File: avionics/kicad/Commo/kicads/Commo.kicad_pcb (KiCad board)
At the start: 4 copper layers, 55 x 35 mm, 88 parts, among them U1 ByA 100nF +3V3 U1-VDDA Bypass, U1 ByB 100nF +3V3 U1-VDD Bypass

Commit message: docs(avionics): Wurth usage notice + uncrewed-only statement on 5 boards; catalogue REF-SENSOR-022..040
Owner decision 2026-09-26: retain the Wurth parts. The Wurth datasheet
usage notice is quoted verbatim [REF-SENSOR-028: Wurth 749010012A data
sheet rev 004.000 p.1] with an 'intended for use only on uncrewed
aircraft' statement in each Wurth-bearing board's .md, as a schematic
text item and PCB Cmts.User text, and in title-block comments 8/9
(tools/add_board_notices.py, idempotent). ERC/DRC/parity counts
unchanged on all five boards (kicad-cli 9.0.2).

REFERENCES.md: REF-SENSOR-022/023/025-030/033/038/040 were cited by
board schematics and generator scripts but never catalogued; entries
added with URLs validated 2026-09-26, unreachable ones marked
'requires verification'.

AI-authored: Claude Opus 5.5 (Anthropic).

Co-Authored-By: Claude Opus 5.5 <noreply@anthropic.com>
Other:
- board text added: "WÜRTH ELEKTRONIK USAGE NOTICE (verbatim, 749010012A data sheet rev 004.000 p.1; applies to Würth parts on this board: 749010012A, 742792510, 742792512): This electronic component has been designed and developed for usage in general electronic equipment only. This product is not authorized for use in equipment where a higher safety standard and reliability standard is especially required or where 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"
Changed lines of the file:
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@@
 		(comment 4 "EMI hardening: SRF2012 CMC + PRTR5V0U2X TVS + Wuerth 742792512 FB + X2Y 4.7nF cap")
 		(comment 5 "Hull: misubisu CC BY 4.0 | Firefly/Serenity fan-work, not officially licensed")
+		(comment 8 "Wurth parts (749010012A, 742792510, 742792512): see Wurth usage notice on this page [USAGE-NOTICE-2026-09-26]")
+		(comment 9 "Intended for use ONLY on uncrewed aircraft")
 	)
 	(layers
@@
 	)
 	(embedded_fonts no)
+	(gr_text "WÜRTH ELEKTRONIK USAGE NOTICE (verbatim, 749010012A data sheet rev 004.000 p.1; applies to Würth\nparts on this board: 749010012A, 742792510, 742792512):\n\nThis electronic component has been designed and developed for usage in general electronic equipment\nonly. This product is not authorized for use in equipment where a higher safety standard and\nreliability standard is especially required or where a failure of the product is reasonably expected\nto cause severe personal injury or death, unless the parties have executed an agreement specifically\ngoverning such use. Moreover Würth Elektronik eiSos GmbH & Co KG products are neither designed nor\nintended for use in areas such as military, aerospace, aviation, nuclear control, submarine,\ntransportation, transportation signal, disaster prevention, medical, public information network\netc.. Würth Elektronik eiSos GmbH & Co KG must be informed about the intent of such usage before the\ndesign-in stage. In addition, sufficient reliability evaluation checks for safety must be performed\non every electronic component which is used in electrical circuits that require high safety and\nreliability functions or performance.\n\nINTENDED USE: The Serenity-UAV avionics, including this board, are intended for use only on uncrewed\naircraft.\n[USAGE-NOTICE-2026-09-26]"
+		(at 160.00 -15.00 0)
+		(layer "Cmts.User")
+		(effects (font (size 0.8 0.8) (thickness 0.1)) (justify left top))
+	)
 )

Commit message: fix(avionics): TLV62569 -> TLV62569PDRLR and TLV75725 -> TLV75725PDRVR package swaps; regulator circuit fixes; stale-component cleanup
Owner-approved swaps (2026-09-26, avionics/WBS.md U7.1e) using the
datasheet-verified SecureControllers library via ${SECURE_CONTROLLERS_LIB}:
- CAN-PERIPH-GW-1 U_REG_3V3, Observer U_REG_3V3/U_REG_1V2, Flight
  Engineer U_REG_3V3_H -> TLV62569PDRLR (SOT-563, 1.6 x 1.6 mm).
  Pins remapped by name; the old symbols had FB/PG swapped (gateway,
  Observer) or sat on a 3-pad SOT-23 (Flight Engineer).
- Observer U_REG_2V5 -> TLV75725PDRVR (WSON-6 2x2, EP to GND).
- Feedback dividers per TLV62569 Sec. 8.2.2.2 Eq. 2 (VFB 0.6 V):
  gateway 10k/20k (0.9 V!) -> 453k/100k = 3.318 V; Observer placeholders
  -> 453k/100k (3V3) and 100k/100k (1V2).
- Flight Engineer: EN was tied to its own 3V3 output and FB straight to
  +3V3 (would regulate at 0.6 V); EN -> +5V, added R_H_FBT 453k /
  R_H_FBB 100k. Parity 2 -> 0, ERC 0.
- tools/kicad_prune_stale.py: parity-driven removal of stale electrical
  footprints and only the copper they orphan; mounting holes are marked
  board_only + renumbered (Commo parity 93 -> 86, Observer 21 -> 17).
- New tools kicad_relink.py / kicad_add_part.py / kicad_set_value.py;
  SecureControllers entries added to every board's lib tables.

Sources: TI TLV62569 (SLVSDG1C) Pin Functions, Sec. 8.2.2.2; TI TLV757P
Fig. 4-3, Pin Functions, DRV0006A.

AI-authored: Claude Opus 5.5 (Anthropic).

Co-Authored-By: Claude Opus 5.5 <noreply@anthropic.com>
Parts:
- gave numbers to parts that had none: 4
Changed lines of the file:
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@@
 	(footprint "MountingHole:MountingHole_2.7mm_M2.5"
 		(layer "F.Cu")
+		(attr board_only)
 		(at 102.5 102.5)
-		(property "Reference" ""
+		(property "Reference" "MH1"
 			(at 0 0 0)
 			(layer "F.SilkS")
@@
 	(footprint "MountingHole:MountingHole_2.7mm_M2.5"
 		(layer "F.Cu")
+		(attr board_only)
 		(at 152.5 102.5)
-		(property "Reference" ""
+		(property "Reference" "MH2"
 			(at 0 0 0)
 			(layer "F.SilkS")
@@
 	(footprint "MountingHole:MountingHole_2.7mm_M2.5"
 		(layer "F.Cu")
+		(attr board_only)
 		(at 102.5 132.5)
-		(property "Reference" ""
+		(property "Reference" "MH3"
 			(at 0 0 0)
 			(layer "F.SilkS")
@@
 	(footprint "MountingHole:MountingHole_2.7mm_M2.5"
 		(layer "F.Cu")
+		(attr board_only)
 		(at 152.5 132.5)
-		(property "Reference" ""
+		(property "Reference" "MH4"
 			(at 0 0 0)
 			(layer "F.SilkS")

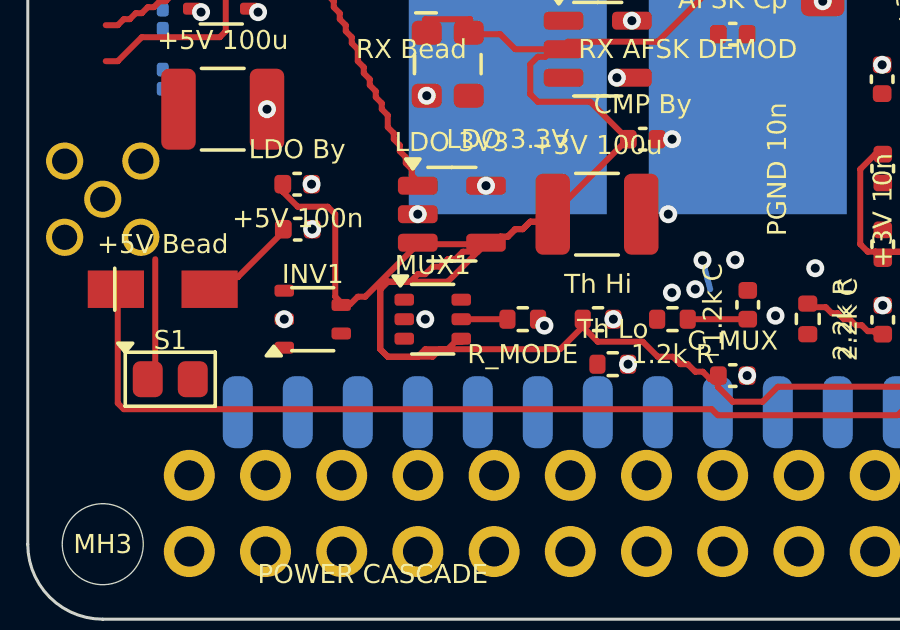
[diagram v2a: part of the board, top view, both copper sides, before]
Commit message: fix(commo): MUX1 -> SN74LVC1G3157DRYR rewired per datasheet; add RF-ESD/BJT candidate datasheets
MUX1 had +3V3 on pin 4 and MODE_SEL on pin 5 (matches neither the '157
nor the '3157). Owner decision 2026-09-26: SN74LVC1G3157DRYR (USON-6,
1.45 x 1.0 mm), rewired per TI SCES424O (B1=UART_RX_F, B2=SBUS_OUT,
A=UART_RX_MUX, S=MODE_SEL, VCC=+3V3) via kicad_relink.py --rewire; GND
stitching via moved clear of the package. Commo ERC 0; parity 86 -> 85.

kicad_relink.py: --rewire mode; adds a missing Footprint property on the
instance (Commo instances had none, so parity saw an empty footprint).

Datasheets fetched for the antenna-TVS and PA-driver replacement
decisions: TI ESD501/601/701/801, Nexperia PESD5V0F1BL/PESD5V0X1BL,
Infineon ESD101-B1 (Rev 1.4), Nexperia PMBT2222A / MMBT2222A.

AI-authored: Claude Opus 5.5 (Anthropic).

Co-Authored-By: Claude Opus 5.5 <noreply@anthropic.com>
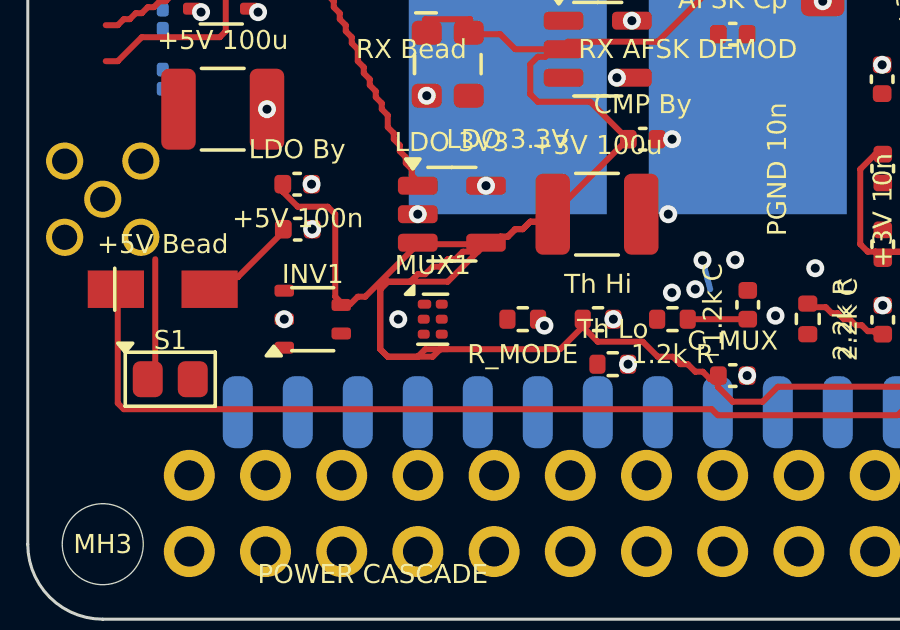
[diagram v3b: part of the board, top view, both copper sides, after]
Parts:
- MUX1: value SN74LVC1G157 SC-70-6 2:1MUX UART/SBUS Select -> SN74LVC1G3157DRYR; footprint SOT-363_SC-70-6 -> Package_SON:Texas_USON-6_1x1.45mm_P0.5mm_SMD
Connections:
- MUX1 pad 1: UART_RX_F -> SBUS_OUT
- MUX1 pad 3: UART_RX_MUX -> UART_RX_F
- MUX1 pad 4: +3V3 -> UART_RX_MUX
- MUX1 pad 5: MODE_SEL -> +3V3
- MUX1 pad 6: SBUS_OUT -> MODE_SEL
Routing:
- net MODE_SEL: track 1.60 -> 0.00 mm
- net +3V3: track 235.8 -> 235.2 mm

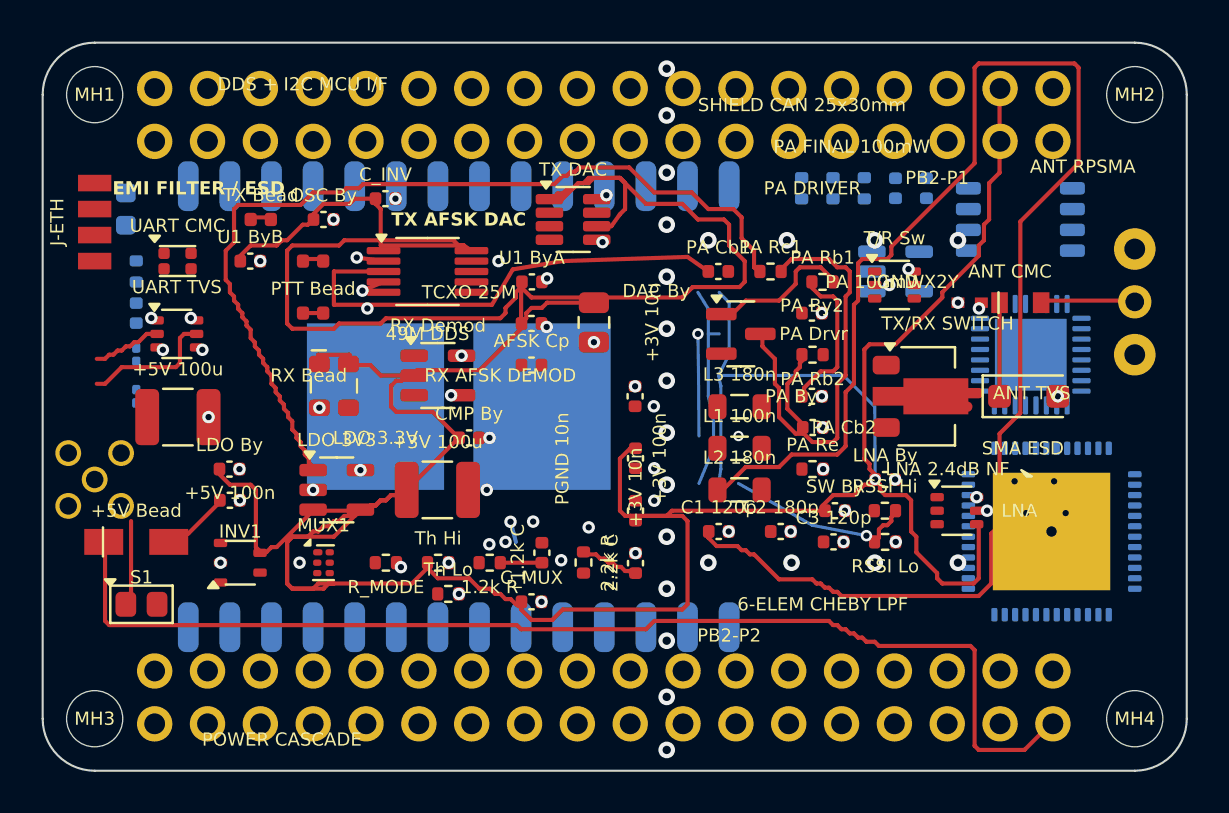
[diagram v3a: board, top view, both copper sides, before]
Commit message: fix(avionics): antenna TVS -> ESD101-B1-02ELS, PA driver -> PMBT2222A; atomic + back-side relink
Owner decisions 2026-09-26 (avionics/WBS.md U7.1j):
- TACCO D-ANT-WIOE5 / D-ANT-RADIO and Commo D-ANT-SIK: deprecated
  RCLAMP0502B -> Infineon ESD101-B1-02ELS (0.1 pF, TSSLP-2-4). The
  proposed RClamp0504FA (3 pF) was rejected for 50-ohm antenna ports
  (0.7 dB at 915 MHz, 3.7-8.8 dB at 2.4/5 GHz). D-ANT-SIK relocated
  beside J-ANT-SIK (old pad 1 overlapped the MH3 hole).
- Commo PA Drvr: MMBT2222A -> Nexperia PMBT2222A (same pinout).
- TACCO.md / Commo.md RF-ESD and BOM text rewritten; unverified 0.15 pF
  RCLAMP claim removed.
- kicad_relink.py: writes schematic and PCB only if both edits succeed;
  supports back-side footprints (local y mirrored, F->B layers).
TACCO: ERC 0, parity 0. Commo: ERC 0, parity 85 -> 83.

AI-authored: Claude Opus 5.5 (Anthropic).

Co-Authored-By: Claude Opus 5.5 <noreply@anthropic.com>
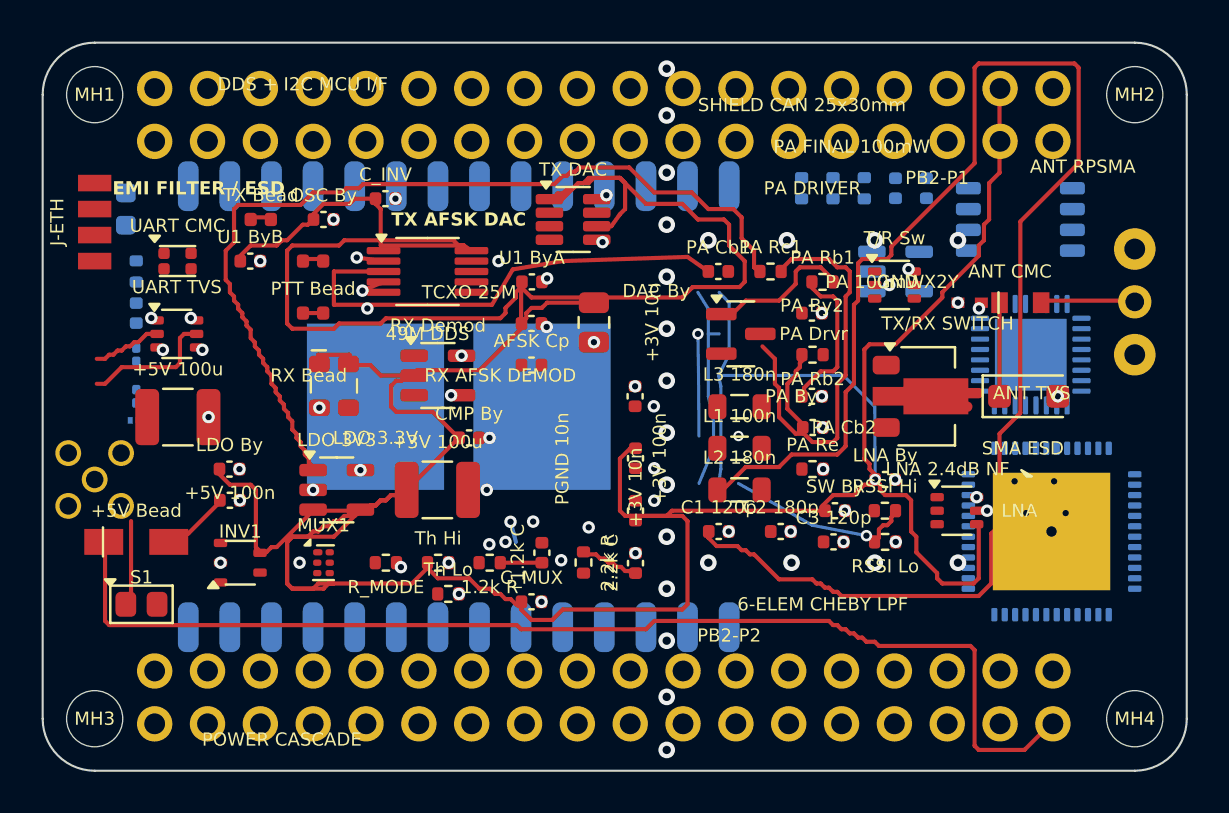
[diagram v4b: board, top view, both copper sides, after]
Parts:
- D-ANT-SIK: value RCLAMP0502B -> ESD101-B1-02ELS; footprint RCLAMP0502B_SOD882 -> SecureControllers:Infineon_TSSLP-2-4_0.62x0.32mm
- PA Drvr: value MMBT2222A NPN BJT PA Class-A Driver -> PMBT2222A,215; footprint SOT-23 -> Package_TO_SOT_SMD:SOT-23
- moved D-ANT-SIK 14.8 mm to (104.4, 118.2), turned to 90 degrees
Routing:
- net PA_INT: track 23.9 -> 23.3 mm
- net DDS_RF: track 30.3 -> 29.7 mm
